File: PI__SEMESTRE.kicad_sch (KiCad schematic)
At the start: 36 parts, among them IC1 LMV358IDR, J1 CX90B-16P1, U1 AMS1117, U11 ESP32-S3-WROOM-1, U14 BME688, U9 GUVA-S12SD

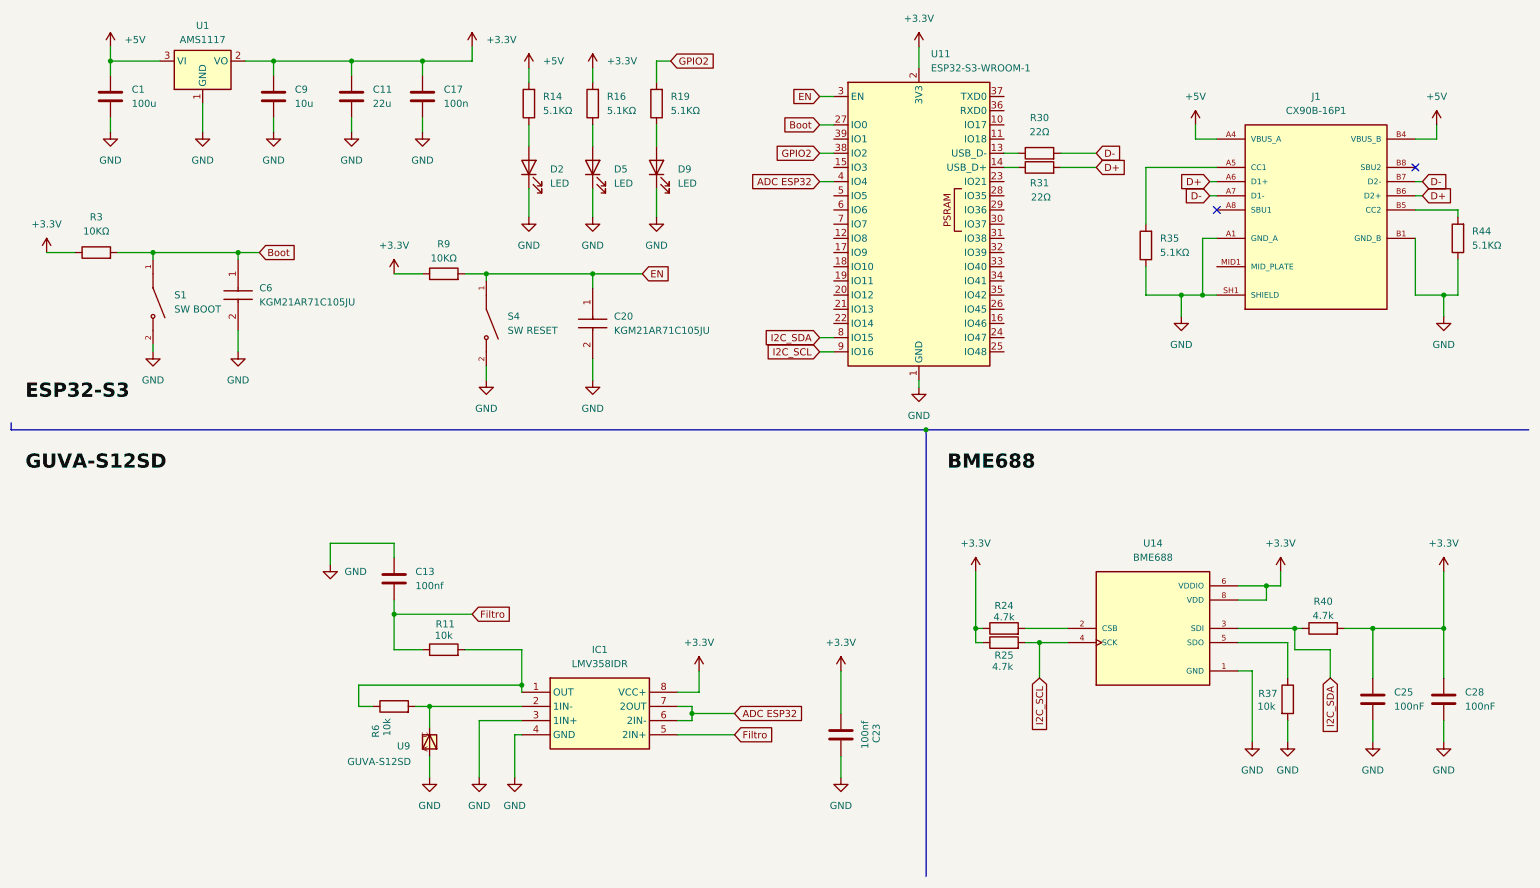
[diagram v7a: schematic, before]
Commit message: se corrigieron muchoss errores tanto que al diseño pcb le hacian falta 4 capacitores porque no tenian huella suministrada, se hicieron cambios de serigrafia, se acomodaron algunos errores tanto de las pistas del usb-c, tambien se agregaron zonas de proteccion contra ruido para los componentes analogos.
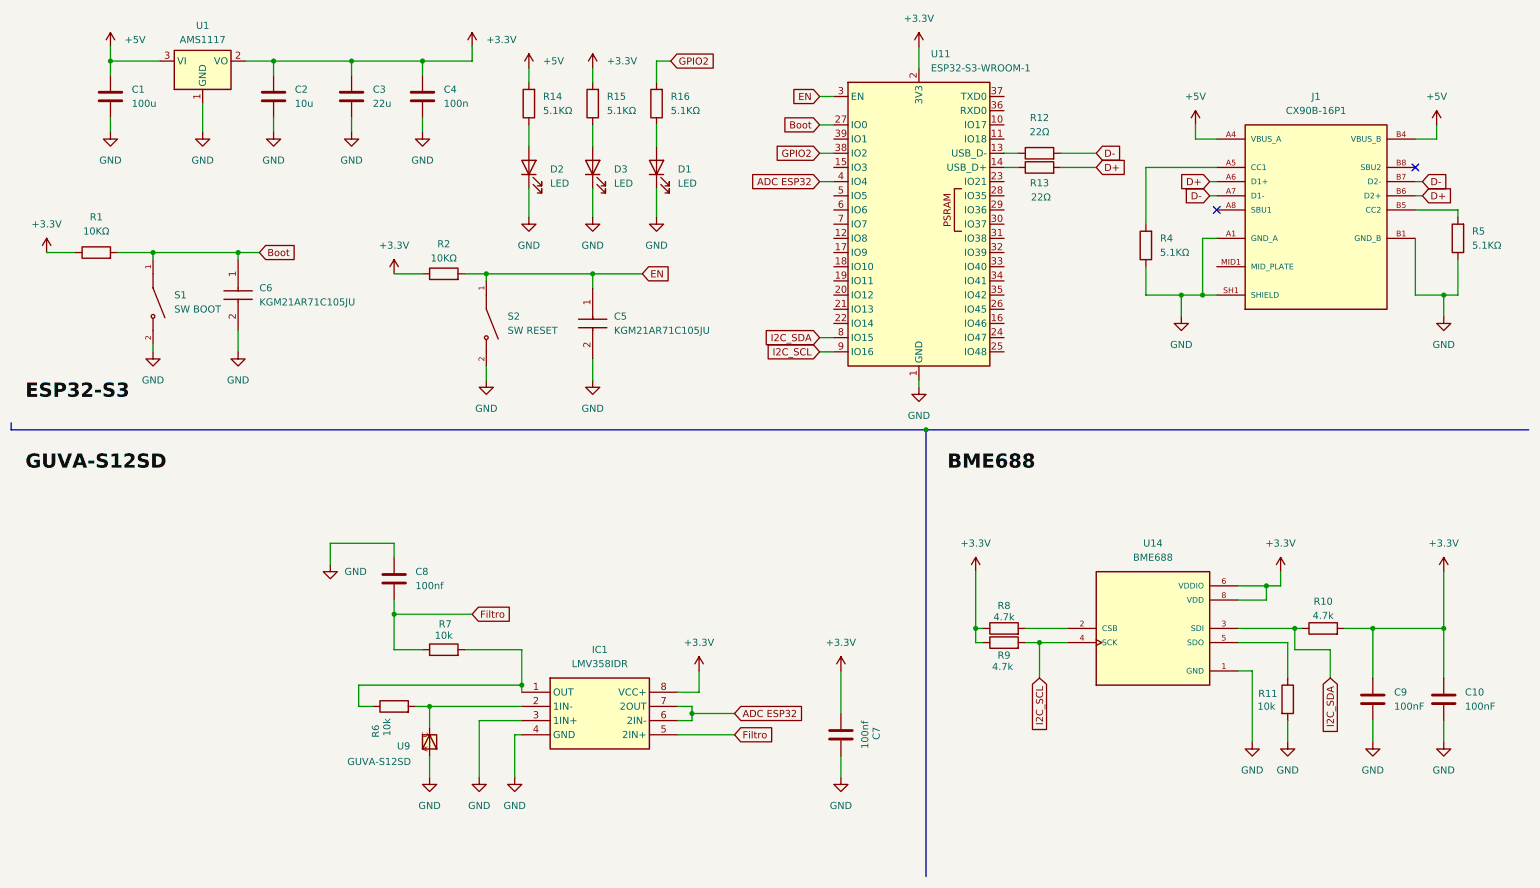
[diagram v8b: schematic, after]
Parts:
- C1: footprint (none) -> Capacitor_SMD:C_0805_2012Metric
- C2: renamed from C9; footprint (none) -> Capacitor_SMD:C_0805_2012Metric
- C3: renamed from C11; footprint (none) -> Capacitor_SMD:C_0805_2012Metric
- C4: renamed from C17; footprint (none) -> Capacitor_SMD:C_0805_2012Metric
- U11: footprint SamacSys_Parts:XCVR_ESP32-S3-WROOM-1U-N16R8 -> ESP32-S3-N16R8:XCVR_ESP32-S3-WROOM-1U-N16R8
- U9: footprint SamacSys_Parts:GUVA-S12SD -> GUVA-S12SD:GUVA-S12SD
- renumbered C28 to C10, C20 to C5, C23 to C7, C13 to C8, C25 to C9, D9 to D1, D5 to D3, R3 to R1, R40 to R10, R37 to R11, R30 to R12, R31 to R13, R16 to R15, R19 to R16, R9 to R2, R35 to R4, R44 to R5, R11 to R7, R24 to R8, R25 to R9, S4 to S2
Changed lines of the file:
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@@
 		(in_pos_files yes)
 		(dnp no)
-		(property "Reference" "R25"
+		(property "Reference" "R9"
 			(at 190.5 128.016 90)
 			(show_name no)
@@
 			(project "PI__SEMESTRE"
 				(path "/8c7ed7b6-4041-4e35-a16c-8ebc40739963"
-					(reference "R25")
+					(reference "R9")
 					(unit 1)
 				)
@@
 		(dnp no)
 		(fields_autoplaced yes)
-		(property "Reference" "R19"
+		(property "Reference" "R16"
 			(at 130.81 27.9399 0)
 			(show_name no)
@@
 			(project "PI__SEMESTRE"
 				(path "/8c7ed7b6-4041-4e35-a16c-8ebc40739963"
-					(reference "R19")
+					(reference "R16")
 					(unit 1)
 				)
@@
 		(dnp no)
 		(fields_autoplaced yes)
-		(property "Reference" "C25"
+		(property "Reference" "C9"
 			(at 260.35 134.6199 0)
 			(show_name no)
@@
 			(project "PI__SEMESTRE"
 				(path "/8c7ed7b6-4041-4e35-a16c-8ebc40739963"
-					(reference "C25")
+					(reference "C9")
 					(unit 1)
 				)
@@
 		(dnp no)
 		(fields_autoplaced yes)
-		(property "Reference" "C13"
+		(property "Reference" "C8"
 			(at 85.09 113.0299 0)
 			(show_name no)
@@
 			(project "PI__SEMESTRE"
 				(path "/8c7ed7b6-4041-4e35-a16c-8ebc40739963"
-					(reference "C13")
+					(reference "C8")
 					(unit 1)
 				)
@@
 			)
 		)
-		(property "Footprint" ""
+		(property "Footprint" "Capacitor_SMD:C_0805_2012Metric"
 			(at 31.4452 31.75 0)
 			(hide yes)
@@
 		(dnp no)
 		(fields_autoplaced yes)
-		(property "Reference" "R44"
+		(property "Reference" "R5"
 			(at 274.32 52.0699 0)
 			(show_name no)
@@
 			(project "PI__SEMESTRE"
 				(path "/8c7ed7b6-4041-4e35-a16c-8ebc40739963"
-					(reference "R44")
+					(reference "R5")
 					(unit 1)
 				)
@@
 		(dnp no)
 		(fields_autoplaced yes)
-		(property "Reference" "S4"
+		(property "Reference" "S2"
 			(at 101.6 67.3099 90)
 			(show_name no)
@@
 			(project "PI__SEMESTRE"
 				(path "/8c7ed7b6-4041-4e35-a16c-8ebc40739963"
-					(reference "S4")
+					(reference "S2")
 					(unit 1)
 				)
@@
 			)
 		)
-		(property "Footprint" "SamacSys_Parts:XCVR_ESP32-S3-WROOM-1U-N16R8"
+		(property "Footprint" "ESP32-S3-N16R8:XCVR_ESP32-S3-WROOM-1U-N16R8"
 			(at 175.26 48.26 0)
 			(hide yes)
@@
 		(dnp no)
 		(fields_autoplaced yes)
-		(property "Reference" "R16"
+		(property "Reference" "R15"
 			(at 119.38 27.9399 0)
 			(show_name no)
@@
 			(project "PI__SEMESTRE"
 				(path "/8c7ed7b6-4041-4e35-a16c-8ebc40739963"
-					(reference "R16")
+					(reference "R15")
 					(unit 1)
 				)
@@
 		(dnp no)
 		(fields_autoplaced yes)
-		(property "Reference" "C11"
+		(property "Reference" "C3"
 			(at 77.47 26.6699 0)
 			(show_name no)
@@
 			)
 		)
-		(property "Footprint" ""
+		(property "Footprint" "Capacitor_SMD:C_0805_2012Metric"
 			(at 74.6252 31.75 0)
 			(hide yes)
@@
 			(project "PI__SEMESTRE"
 				(path "/8c7ed7b6-4041-4e35-a16c-8ebc40739963"
-					(reference "C11")
+					(reference "C3")
 					(unit 1)
 				)
@@
 		(in_pos_files yes)
 		(dnp no)
-		(property "Reference" "R37"
+		(property "Reference" "R11"
 			(at 237.744 134.874 0)
 			(show_name no)
@@
 			(project "PI__SEMESTRE"
 				(path "/8c7ed7b6-4041-4e35-a16c-8ebc40739963"
-					(reference "R37")
+					(reference "R11")
 					(unit 1)
 				)
@@
 		(in_pos_files yes)
 		(dnp no)
-		(property "Reference" "R40"
+		(property "Reference" "R10"
 			(at 247.65 118.364 90)
 			(show_name no)
@@
 			(project "PI__SEMESTRE"
 				(path "/8c7ed7b6-4041-4e35-a16c-8ebc40739963"
-					(reference "R40")
+					(reference "R10")
 					(unit 1)
 				)
@@
 		(in_pos_files yes)
 		(dnp no)
-		(property "Reference" "R31"
+		(property "Reference" "R13"
 			(at 196.85 43.434 90)
 			(show_name no)
@@
 			(project "PI__SEMESTRE"
 				(path "/8c7ed7b6-4041-4e35-a16c-8ebc40739963"
-					(reference "R31")
+					(reference "R13")
 					(unit 1)
 				)
@@
 		(dnp no)
 		(fields_autoplaced yes)
-		(property "Reference" "D5"
+		(property "Reference" "D3"
 			(at 120.65 40.9574 90)
 			(show_name no)
@@
 			(project "PI__SEMESTRE"
 				(path "/8c7ed7b6-4041-4e35-a16c-8ebc40739963"
-					(reference "D5")
+					(reference "D3")
 					(unit 1)
 				)
@@
 		(dnp no)
 		(fields_autoplaced yes)
-		(property "Reference" "R3"
+		(property "Reference" "R1"
 			(at 27.94 49.53 90)
 			(show_name no)
@@
 			(project "PI__SEMESTRE"
 				(path "/8c7ed7b6-4041-4e35-a16c-8ebc40739963"
-					(reference "R3")
+					(reference "R1")
 					(unit 1)
 				)
@@
 		(in_pos_files yes)
 		(dnp no)
-		(property "Reference" "C23"
+		(property "Reference" "C7"
 			(at 167.64 141.986 90)
 			(show_name no)
@@
 			(project "PI__SEMESTRE"
 				(path "/8c7ed7b6-4041-4e35-a16c-8ebc40739963"
-					(reference "C23")
+					(reference "C7")
 					(unit 1)
 				)
@@
 		(in_pos_files yes)
 		(dnp no)
-		(property "Reference" "R11"
+		(property "Reference" "R7"
 			(at 90.424 122.428 90)
 			(show_name no)
@@
 			(project "PI__SEMESTRE"
 				(path "/8c7ed7b6-4041-4e35-a16c-8ebc40739963"
-					(reference "R11")
+					(reference "R7")
 					(unit 1)
 				)
@@
 		(dnp no)
 		(fields_autoplaced yes)
-		(property "Reference" "C20"
+		(property "Reference" "C5"
 			(at 120.65 67.3099 90)
 			(show_name no)
@@
 			(project "PI__SEMESTRE"
 				(path "/8c7ed7b6-4041-4e35-a16c-8ebc40739963"
-					(reference "C20")
+					(reference "C5")
 					(unit 1)
 				)
@@
 		(dnp no)
 		(fields_autoplaced yes)
-		(property "Reference" "D9"
+		(property "Reference" "D1"
 			(at 132.08 40.9574 90)
 			(show_name no)
@@
 			(project "PI__SEMESTRE"
 				(path "/8c7ed7b6-4041-4e35-a16c-8ebc40739963"
-					(reference "D9")
+					(reference "D1")
 					(unit 1)
 				)
@@
 		(dnp no)
 		(fields_autoplaced yes)
-		(property "Reference" "C28"
+		(property "Reference" "C10"
 			(at 273.05 134.6199 0)
 			(show_name no)
@@
 			(project "PI__SEMESTRE"
 				(path "/8c7ed7b6-4041-4e35-a16c-8ebc40739963"
-					(reference "C28")
+					(reference "C10")
 					(unit 1)
 				)
@@
 		(dnp no)
 		(fields_autoplaced yes)
-		(property "Reference" "C17"
+		(property "Reference" "C4"
 			(at 90.17 26.6699 0)
 			(show_name no)
@@
 			)
 		)
-		(property "Footprint" ""
+		(property "Footprint" "Capacitor_SMD:C_0805_2012Metric"
 			(at 87.3252 31.75 0)
 			(hide yes)
@@
 			(project "PI__SEMESTRE"
 				(path "/8c7ed7b6-4041-4e35-a16c-8ebc40739963"
-					(reference "C17")
+					(reference "C4")
 					(unit 1)
 				)
@@
 		(dnp no)
 		(fields_autoplaced yes)
-		(property "Reference" "R35"
+		(property "Reference" "R4"
 			(at 218.44 53.3399 0)
 			(show_name no)
@@
 			(project "PI__SEMESTRE"
 				(path "/8c7ed7b6-4041-4e35-a16c-8ebc40739963"
-					(reference "R35")
+					(reference "R4")
 					(unit 1)
 				)
@@
 			)
 		)
-		(property "Footprint" "SamacSys_Parts:GUVA-S12SD"
+		(property "Footprint" "GUVA-S12SD:GUVA-S12SD"
 			(at 87.63 143.51 0)
 			(hide yes)
@@
 		(dnp no)
 		(fields_autoplaced yes)
-		(property "Reference" "R30"
+		(property "Reference" "R12"
 			(at 196.85 31.75 90)
 			(show_name no)
@@
 			(project "PI__SEMESTRE"
 				(path "/8c7ed7b6-4041-4e35-a16c-8ebc40739963"
-					(reference "R30")
+					(reference "R12")
 					(unit 1)
 				)
@@
 		(in_pos_files yes)
 		(dnp no)
-		(property "Reference" "R9"
+		(property "Reference" "R2"
 			(at 90.17 54.356 90)
 			(show_name no)
@@
 			(project "PI__SEMESTRE"
 				(path "/8c7ed7b6-4041-4e35-a16c-8ebc40739963"
-					(reference "R9")
+					(reference "R2")
 					(unit 1)
 				)
@@
 		(in_pos_files yes)
 		(dnp no)
-		(property "Reference" "R24"
+		(property "Reference" "R8"
 			(at 190.5 119.126 90)
 			(show_name no)
@@
 			(project "PI__SEMESTRE"
 				(path "/8c7ed7b6-4041-4e35-a16c-8ebc40739963"
-					(reference "R24")
+					(reference "R8")
 					(unit 1)
 				)
@@
 		(dnp no)
 		(fields_autoplaced yes)
-		(property "Reference" "C9"
+		(property "Reference" "C2"
 			(at 63.5 26.6699 0)
 			(show_name no)
@@
 			)
 		)
-		(property "Footprint" ""
+		(property "Footprint" "Capacitor_SMD:C_0805_2012Metric"
 			(at 60.6552 31.75 0)
 			(hide yes)
@@
 			(project "PI__SEMESTRE"
 				(path "/8c7ed7b6-4041-4e35-a16c-8ebc40739963"
-					(reference "C9")
+					(reference "C2")
 					(unit 1)
 				)
